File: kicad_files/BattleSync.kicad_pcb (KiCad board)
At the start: 2 copper layers, 14 parts, among them U1 113991054, U2 DFR0299, U3 AMS1117-3.3

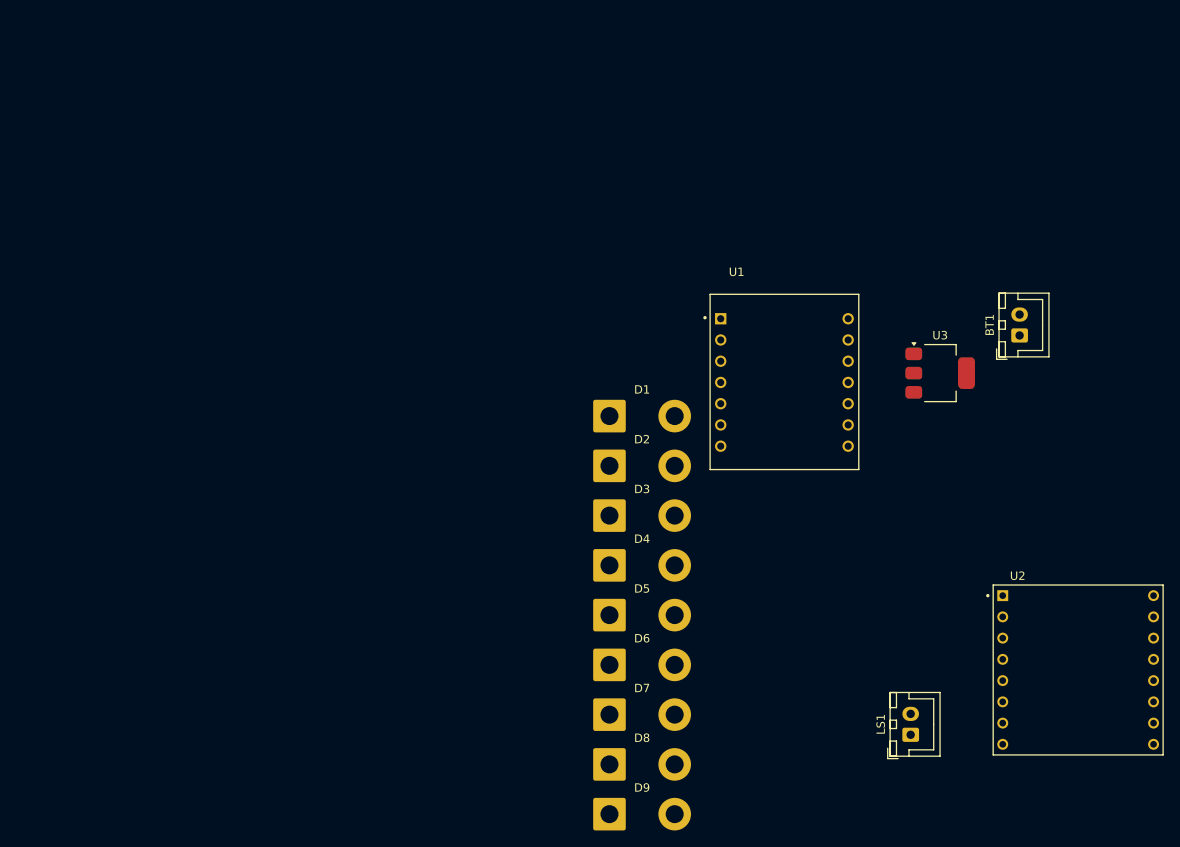
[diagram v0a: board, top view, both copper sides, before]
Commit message: work on updating kicad files with project-level symbols and footprints
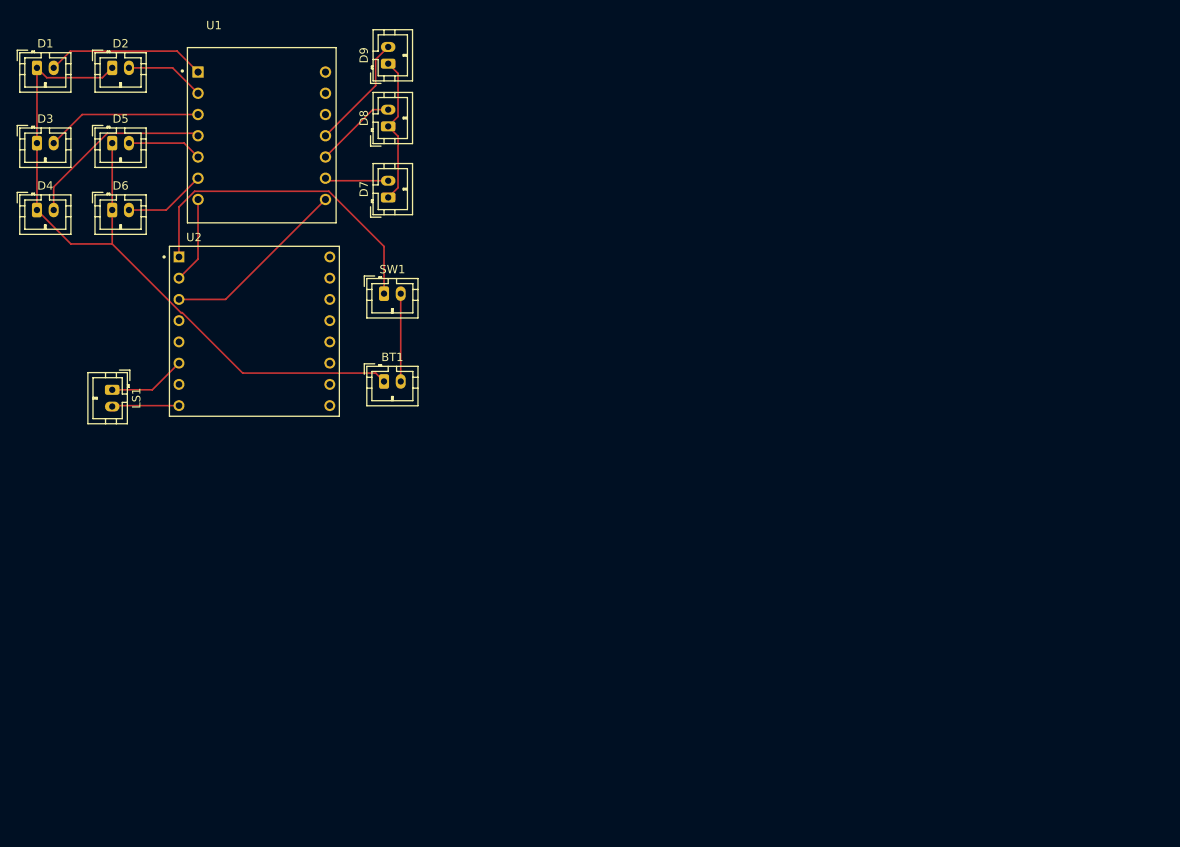
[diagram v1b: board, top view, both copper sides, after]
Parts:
- removed U3: AMS1117-3.3, Package_TO_SOT_SMD:SOT-223-3_TabPin2
- added SW1: SW_SPDT, Connector_JST:JST_PH_B2B-PH-K_1x02_P2.00mm_Vertical, F.Cu at (84.5, 46.5)
- BT1, LS1: footprint Connector_JST:JST_XH_B2B-XH-A_1x02_P2.50mm_Vertical -> Connector_JST:JST_PH_B2B-PH-K_1x02_P2.00mm_Vertical
- D1, D2, D3, D4, D5, D6, D7, D8, D9: footprint Connector_Wire:SolderWire-1.5sqmm_1x02_P7.8mm_D1.7mm_OD3.9mm -> Connector_JST:JST_PH_B2B-PH-K_1x02_P2.00mm_Vertical
- U1: value 113991054 -> ESP32-C3; footprint 113991054:MODULE_113991054 -> Seeeduino xiao ESP32C3 KiCAD Library:MODULE_113991054
- U2: value DFR0299 -> DFPlayer Mini
- moved U2 106.5 mm to (69.0, 51.0)
- moved LS1 104.0 mm to (52.0, 58.0), turned to -90 degrees
- moved D9 93.6 mm to (85.0, 19.0), turned to 90 degrees
- moved D5 82.0 mm to (52.0, 28.5)
- moved D3 81.7 mm to (43.0, 28.5)
- moved D8 80.7 mm to (85.0, 26.5), turned to 90 degrees
- moved D6 80.6 mm to (52.0, 36.5)
- moved D4 80.6 mm to (43.0, 36.5)
- moved D1 80.1 mm to (43.0, 19.5)
- moved BT1 76.2 mm to (84.5, 57.0), turned to 0 degrees
- moved D2 76.2 mm to (52.0, 19.5)
- moved U1 69.1 mm to (69.9, 27.6)
- moved D7 67.3 mm to (85.0, 35.0), turned to 90 degrees
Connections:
- D1 pad 1: Net-(BT1--) -> Net-(BT1-+)
- D2 pad 1: Net-(BT1--) -> Net-(BT1-+)
- D3 pad 1: Net-(BT1--) -> Net-(BT1-+)
- D4 pad 1: Net-(BT1--) -> Net-(BT1-+)
- D5 pad 1: Net-(BT1--) -> Net-(BT1-+)
- D6 pad 1: Net-(BT1--) -> Net-(BT1-+)
- D7 pad 1: Net-(BT1--) -> Net-(BT1-+)
- D8 pad 1: Net-(BT1--) -> Net-(BT1-+)
- D9 pad 1: Net-(BT1--) -> Net-(BT1-+)
- LS1 pad 1: Net-(U2-SPK2) -> Net-(U2-SPK_1)
- LS1 pad 2: Net-(U2-SPK1) -> Net-(U2-SPK_2)
- U1 pad 10: Net-(D9-A) -> Net-(D8-A)
- U1 pad 11: Net-(D8-A) -> Net-(D9-A)
- U1 pad 12: Net-(U1-VCC_3V3) -> unconnected-(U1-3V3-Pad12)
- U1 pad 13: Net-(BT1--) -> unconnected-(U1-GND-Pad13)
- U2 pad 1: Net-(BT1-+) -> Net-(SW1-A)
- U2 pad 10: Net-(BT1--) -> unconnected-(U2-GND-Pad10)
- U2 pad 6: Net-(U2-SPK1) -> Net-(U2-SPK_1)
- U2 pad 7: Net-(BT1--) -> Net-(BT1-+)
- U2 pad 8: Net-(U2-SPK2) -> Net-(U2-SPK_2)
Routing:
- net Net-(BT1-+): track 0.00 -> 107.0 mm
- net Net-(SW1-A): track 0.00 -> 39.6 mm
- net Net-(D4-A): track 0.00 -> 22.8 mm
- net Net-(U1-GPIO20_D7_RX): track 0.00 -> 22.5 mm
- net Net-(D1-A): track 0.00 -> 19.1 mm
- net Net-(D3-A): track 0.00 -> 18.7 mm
- net Net-(D9-A): track 0.00 -> 13.7 mm
- net Net-(BT1--): track 0.00 -> 10.5 mm
- net Net-(U1-GPIO21_D6_TX): track 0.00 -> 10.4 mm
- net Net-(D8-A): track 0.00 -> 9.84 mm
- net Net-(D6-A): track 0.00 -> 9.83 mm
- net Net-(D2-A): track 0.00 -> 9.52 mm
- net Net-(U2-SPK_1): track 0.00 -> 9.30 mm
- net Net-(D5-A): track 0.00 -> 8.95 mm
- net Net-(U2-SPK_2): track 0.00 -> 8.03 mm
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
